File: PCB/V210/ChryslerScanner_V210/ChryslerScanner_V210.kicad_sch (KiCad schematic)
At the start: 3 parts

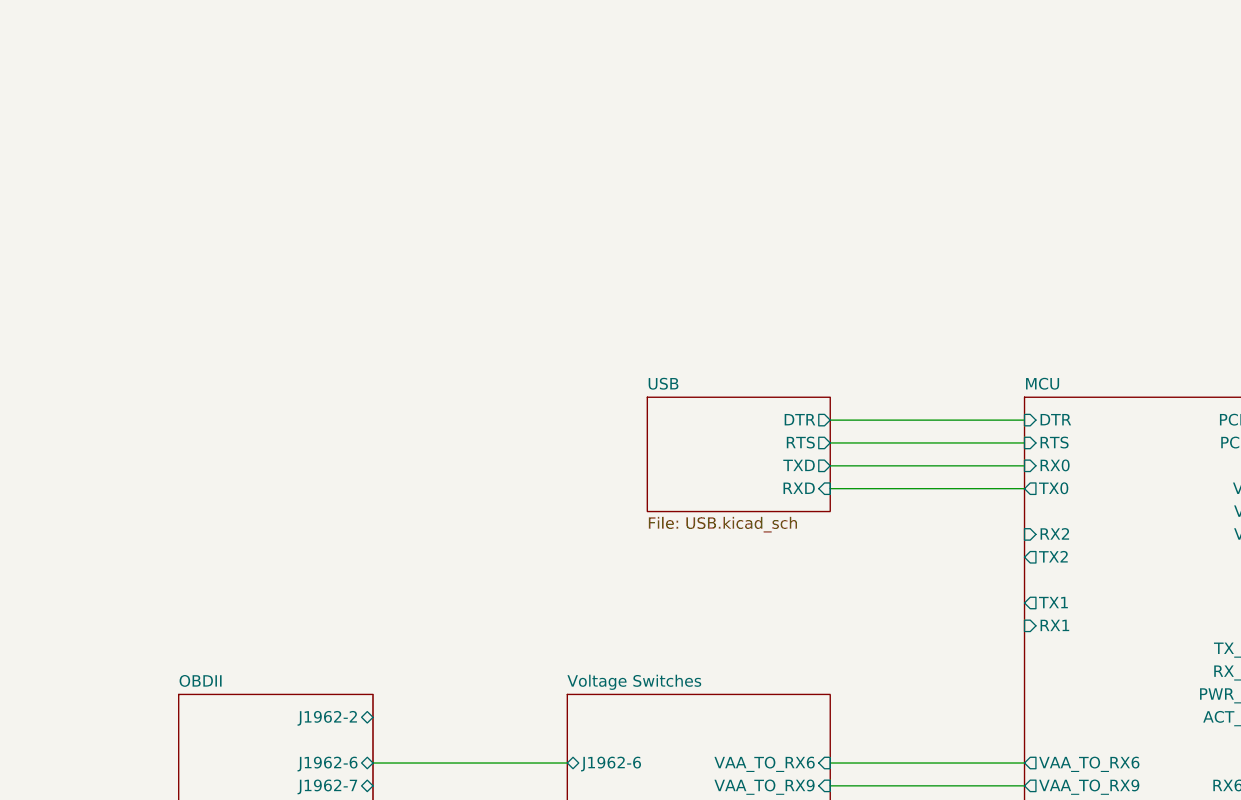
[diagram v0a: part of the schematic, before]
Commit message: Added power supplies. Removed CCD.
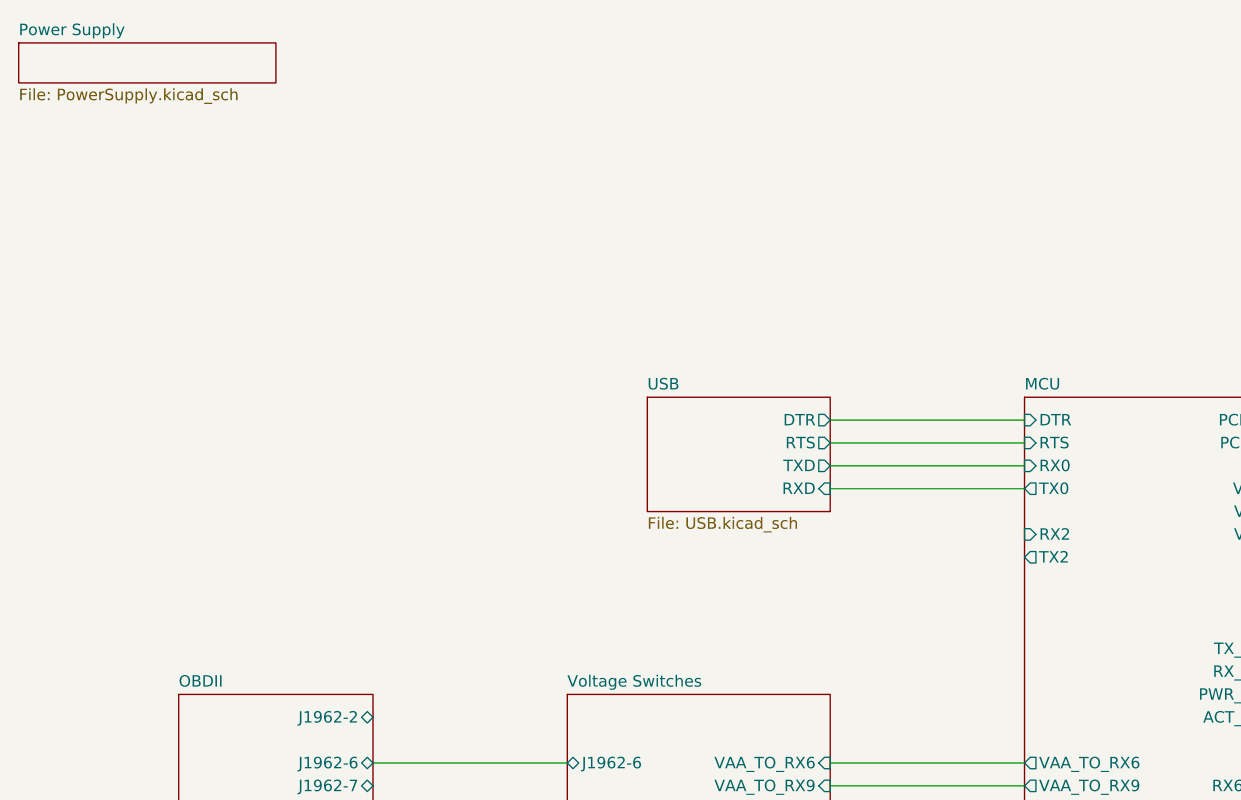
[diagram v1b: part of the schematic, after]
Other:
- added sheet Power Supply (PowerSupply.kicad_sch)
- sheet MCU ports: added none; removed RX1, TX1

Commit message: Completed schematic.
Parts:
- gave numbers to parts that had none: 3
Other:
- added sheet PCI (PCI.kicad_sch)
- added sheet SCI (SCI.kicad_sch)
- sheet MCU ports: added none; removed TBEN
- sheet OBDII ports: added none; removed J1962-11, J1962-3

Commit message: WIP
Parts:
- FID1, FID2, FID3: footprint (none) -> Fiducial:Fiducial_0.5mm_Mask1mm
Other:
- removed sheet Voltage Switches
- sheet MCU ports: added none; removed VAA_TO_RX12, VAA_TO_RX14, VAA_TO_RX6, VAA_TO_RX9, VPP_TO_RX12, VPP_TO_RX14, VPP_TO_RX6, VPP_TO_RX9
- title: Chrysler Scanner -> TJ Diag

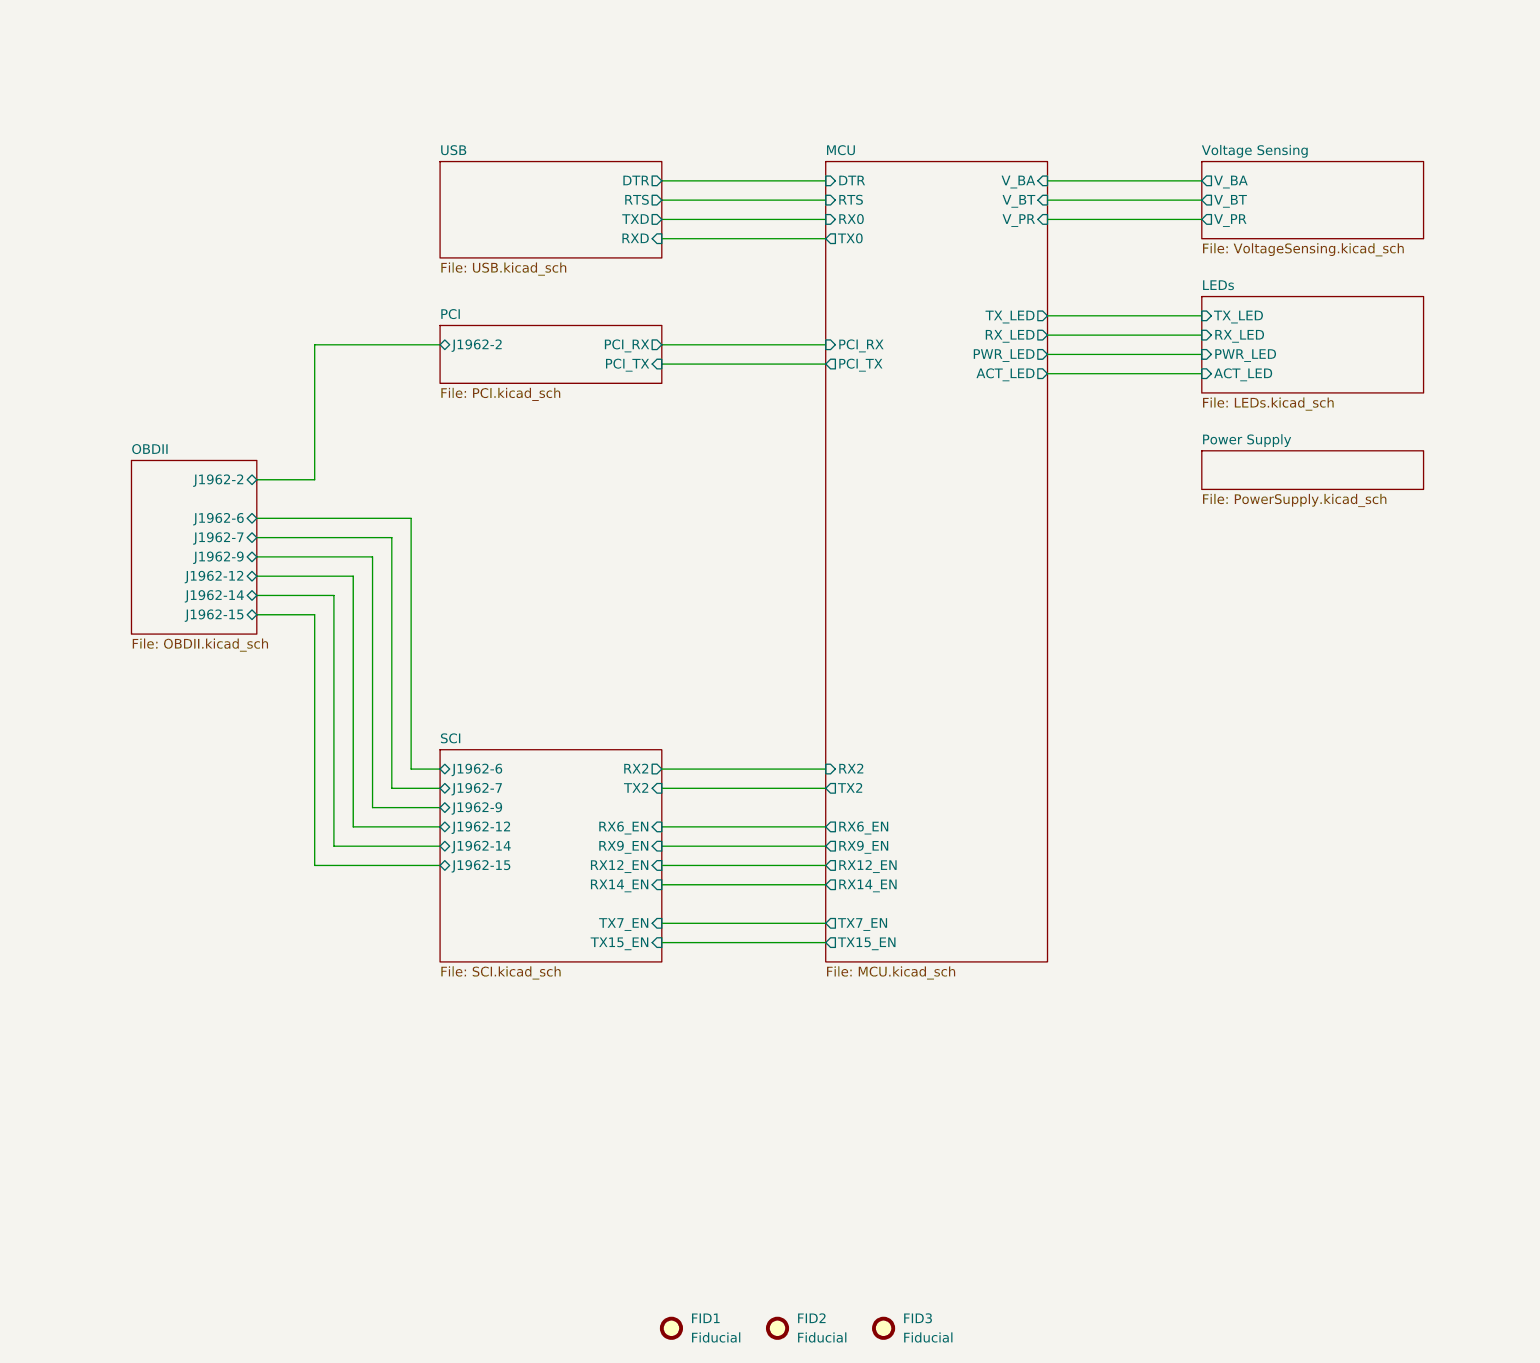
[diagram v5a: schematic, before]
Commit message: Added CCD back in - needed for early TJs.
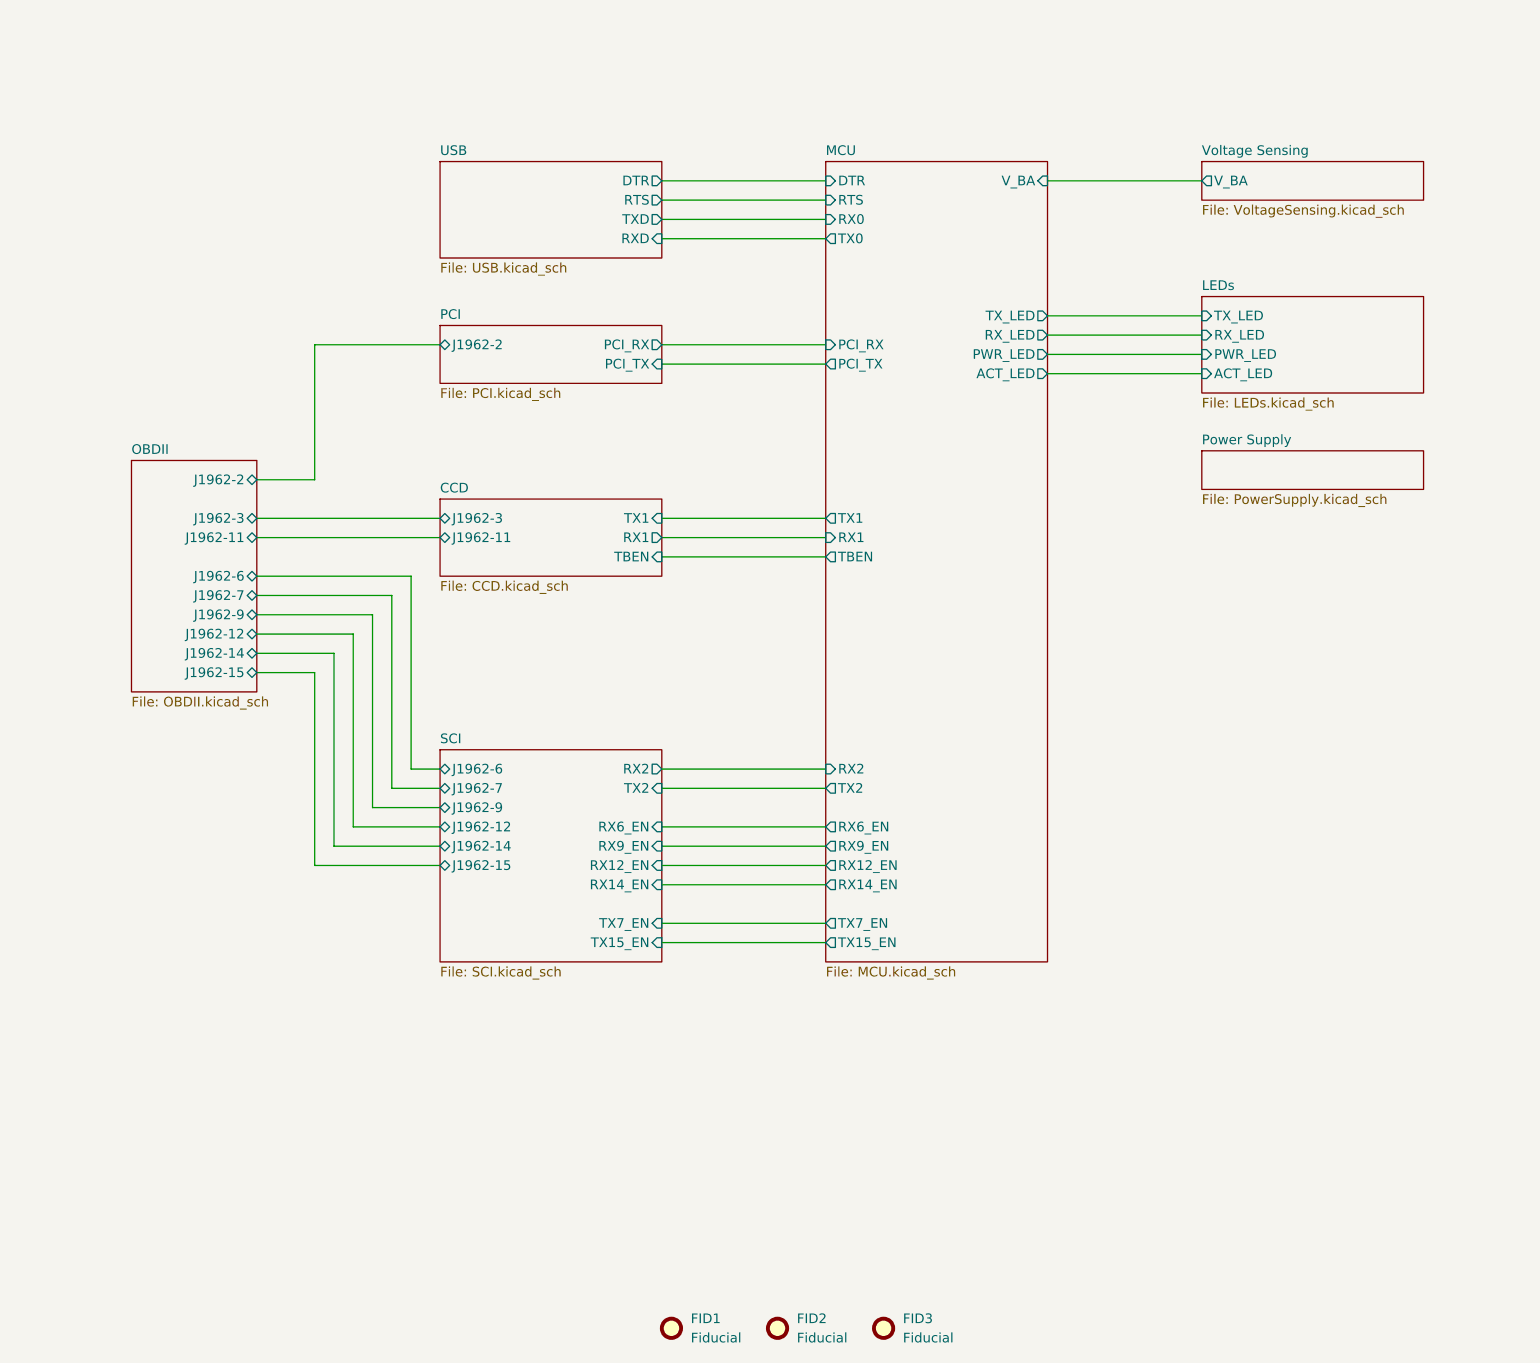
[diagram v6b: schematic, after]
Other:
- added sheet CCD (CCD.kicad_sch)
- sheet MCU ports: added RX1, TBEN, TX1; removed V_BT, V_PR
- sheet OBDII ports: added J1962-11, J1962-3; removed none
- sheet Voltage Sensing ports: added none; removed V_BT, V_PR
